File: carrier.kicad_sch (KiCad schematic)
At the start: 53 parts, among them J1 Conn_02x06_Odd_Even, J10 Conn_01x02, J11 Conn_01x02, J12 AudioJack3_SwitchTR, J2 Conn_01x26, J3 Conn_01x26, J4 TYPE-C-31-M-12, J5 Conn_01x02, J6 Conn_01x02, J7 Conn_01x02, J8 Conn_01x02, J9 Conn_01x02, U1 CARAVEL, U2 W25Q128JVS, U3 LP5907MFX-3.3, U4 LP5907MFX-1.8, U5 LP5907MFX-1.8, U6 LP5907MFX-3.3, U7 TPD2E001DRSR, U8 OPA340NA, U9 OPA340NA, X1 SG-5032CAN

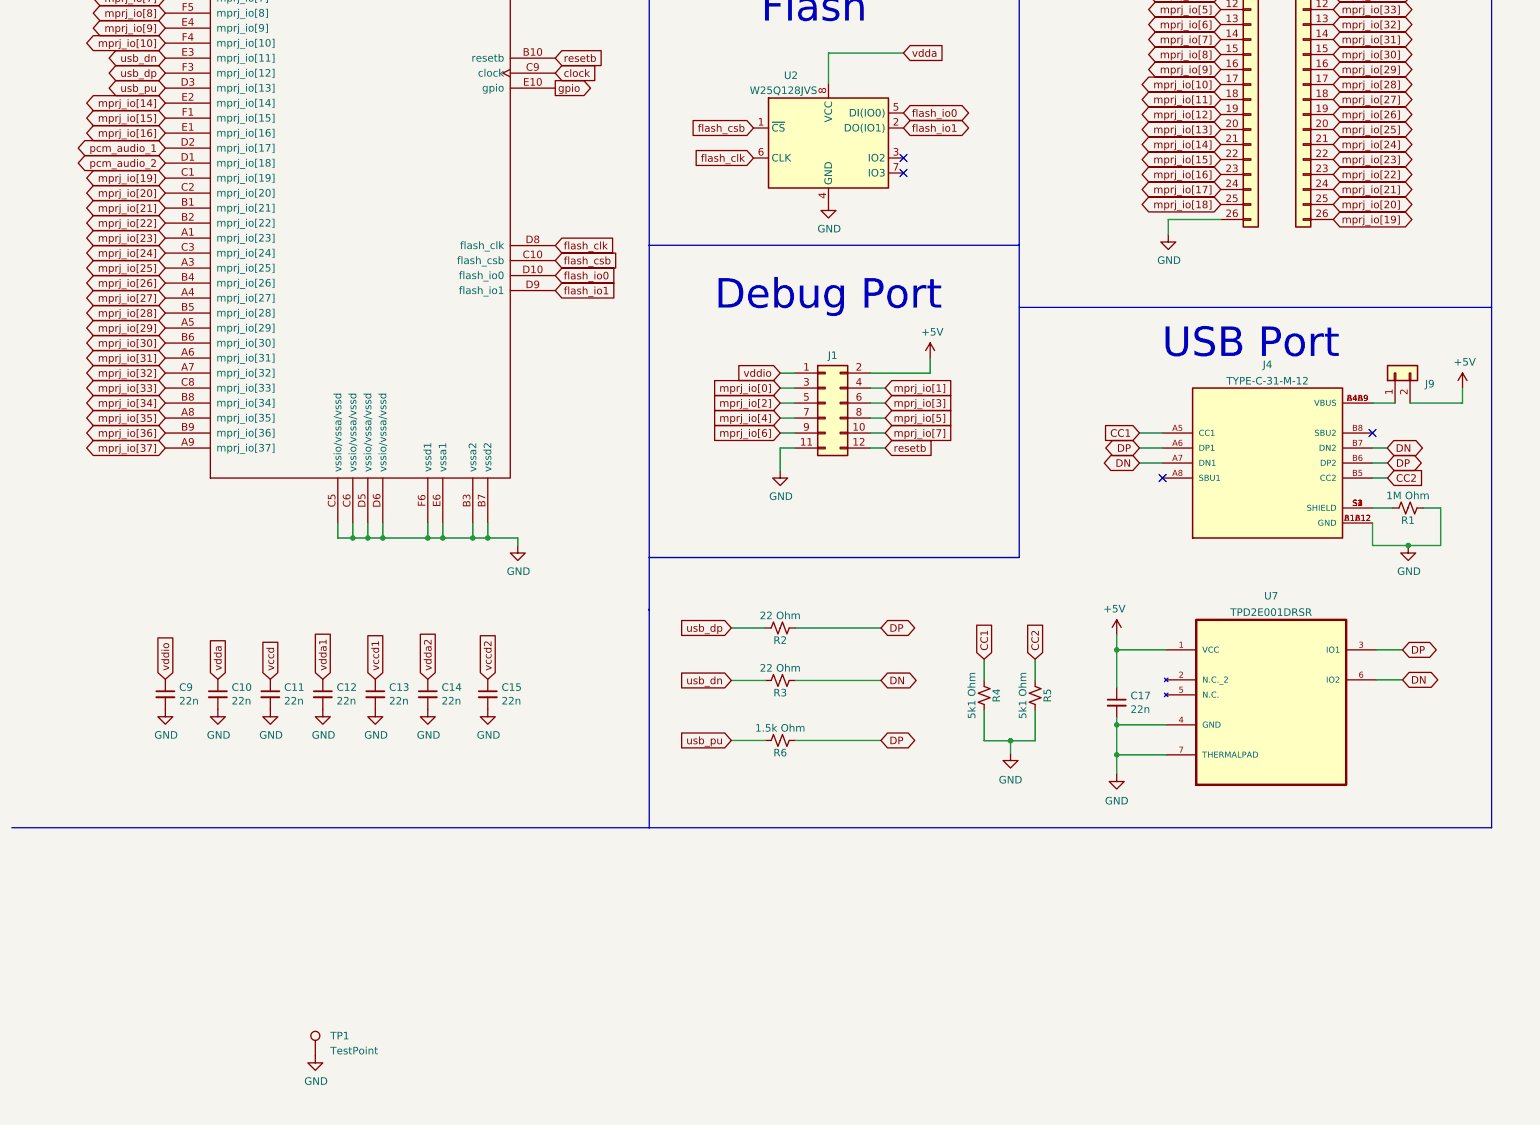
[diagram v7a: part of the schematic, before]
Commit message: Add video connector
May want to use PMOD specific connector numbering to avoid confusion.
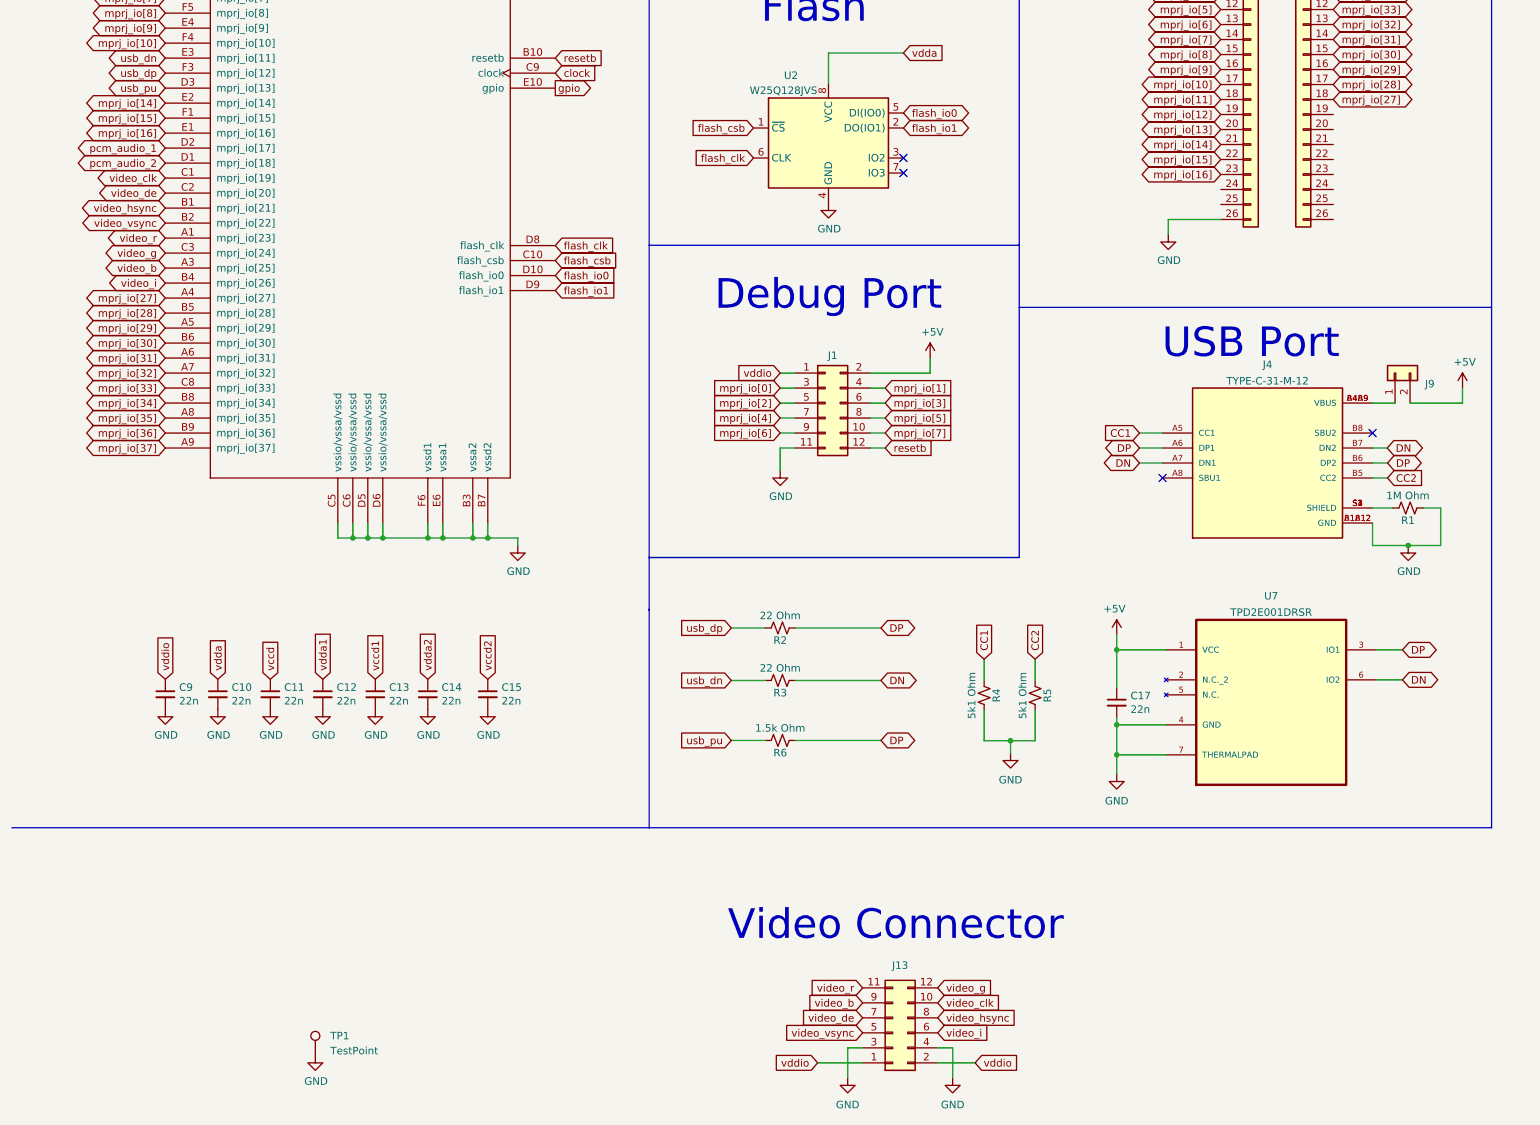
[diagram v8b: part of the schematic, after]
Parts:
- added J13: Conn_02x06_Odd_Even, Connector_PinSocket_2.54mm:PinSocket_2x06_P2.54mm_Horizontal, symbol Connector_Generic:Conn_02x06_Odd_Even
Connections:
- net GND: now also J13.3 (Pin_3), J13.4 (Pin_4)
- net vddio: now also J13.1 (Pin_1), J13.2 (Pin_2)
- net mprj_io[17]: no longer names the net of J2.24 (Pin_24)
- net mprj_io[18]: no longer names the net of J2.25 (Pin_25)
- net mprj_io[19]: no longer names the net of J3.26 (Pin_26)
- net mprj_io[19]: no longer U1.C1 (mprj_io[19])
- net mprj_io[20]: no longer names the net of J3.25 (Pin_25)
- net mprj_io[20]: no longer U1.C2 (mprj_io[20])
- net mprj_io[21]: no longer names the net of J3.24 (Pin_24)
- net mprj_io[21]: no longer U1.B1 (mprj_io[21])
- net mprj_io[22]: no longer names the net of J3.23 (Pin_23)
- net mprj_io[22]: no longer U1.B2 (mprj_io[22])
- net mprj_io[23]: no longer names the net of J3.22 (Pin_22)
- net mprj_io[23]: no longer U1.A1 (mprj_io[23])
- net mprj_io[24]: no longer names the net of J3.21 (Pin_21)
- net mprj_io[24]: no longer U1.C3 (mprj_io[24])
- net mprj_io[25]: no longer names the net of J3.20 (Pin_20)
- net mprj_io[25]: no longer U1.A3 (mprj_io[25])
- net mprj_io[26]: no longer names the net of J3.19 (Pin_19)
- net mprj_io[26]: no longer U1.B4 (mprj_io[26])
- new net video_b: J13.9 (Pin_9), U1.A3 (mprj_io[25])
- new net video_clk: J13.10 (Pin_10), U1.C1 (mprj_io[19])
- new net video_de: J13.7 (Pin_7), U1.C2 (mprj_io[20])
- new net video_g: J13.12 (Pin_12), U1.C3 (mprj_io[24])
- new net video_hsync: J13.8 (Pin_8), U1.B1 (mprj_io[21])
- new net video_i: J13.6 (Pin_6), U1.B4 (mprj_io[26])
- new net video_r: J13.11 (Pin_11), U1.A1 (mprj_io[23])
- new net video_vsync: J13.5 (Pin_5), U1.B2 (mprj_io[22])
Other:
- note added: "Video Connector"
